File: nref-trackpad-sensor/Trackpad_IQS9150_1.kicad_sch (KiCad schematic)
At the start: 44 parts, among them CN1 FPC_6PIN, IC1 IQS9150-000QFR

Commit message: trackpad: pcb traces adjustment for prod
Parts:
- CN1: footprint Trackpad_IQS9150:FPC6PIN -> Connector_FFC-FPC:Hirose_FH12-6S-0.5SH_1x06-1MP_P0.50mm_Horizontal

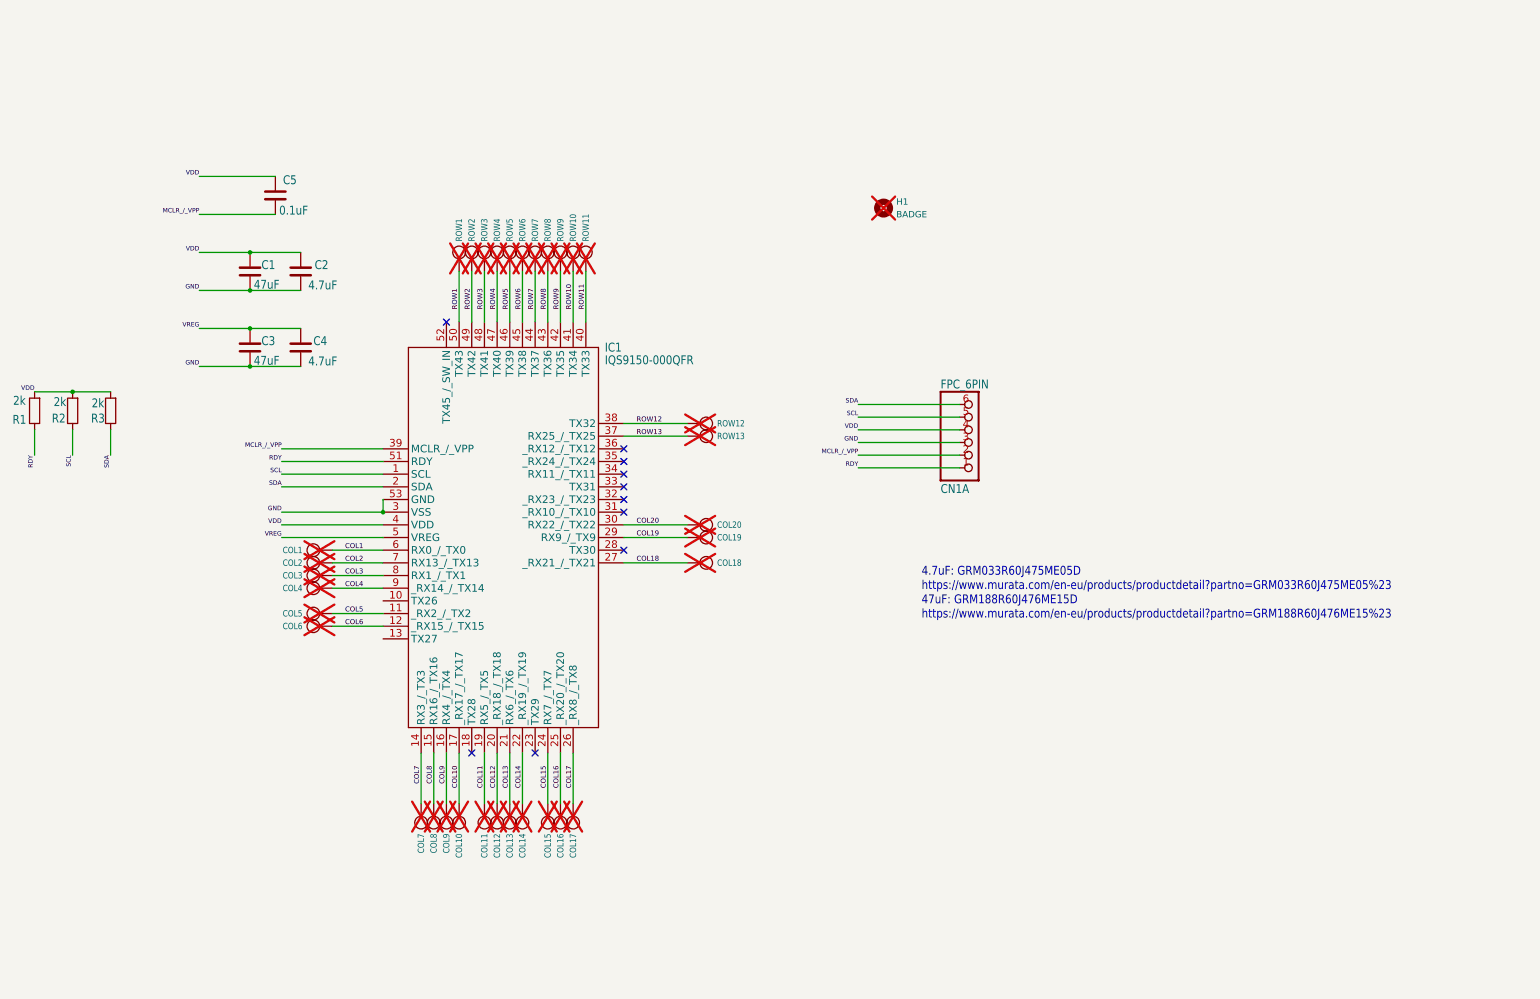
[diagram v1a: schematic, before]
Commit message: clean up major schematics for book
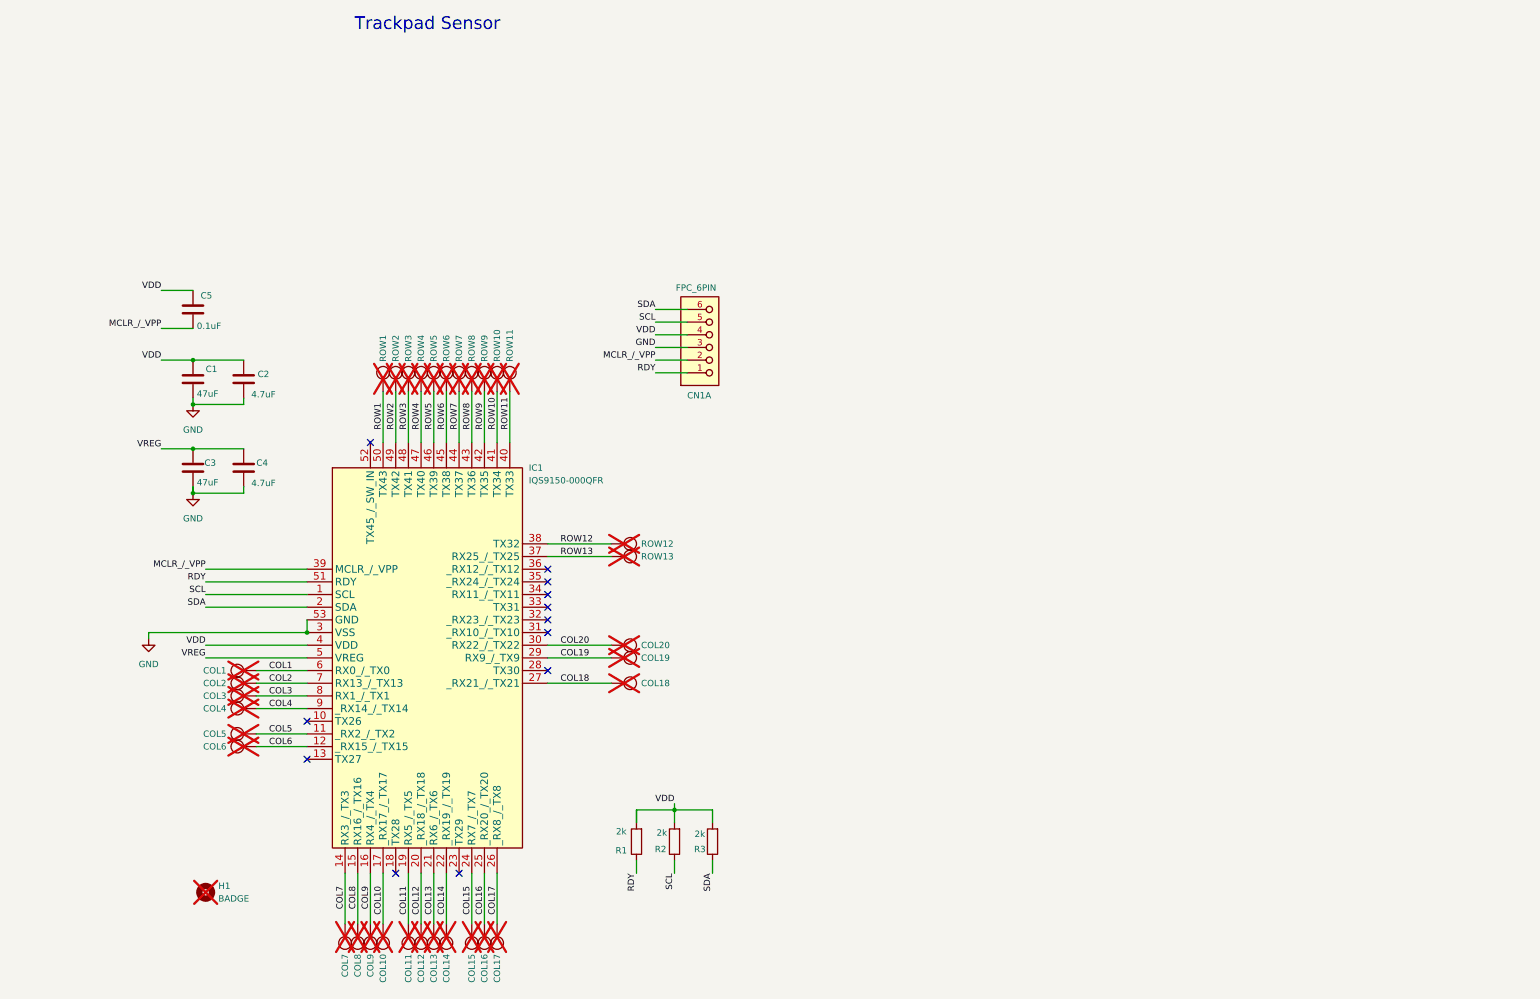
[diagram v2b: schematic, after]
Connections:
- no-connect marks 10 -> 12
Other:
- note added: "Trackpad Sensor"
- note removed: "4.7uF: GRM033R60J475ME05D https://www.murata.com/en-eu/products/productdetail?partno=GRM033R60J475ME05%23 47uF: GRM188R60J476ME15D https://www.murata.com/en-eu/products/productdetail?partno=GRM188R60J476ME15%23"
- company: (none) -> MNT Research GmbH, Copyright 2026
- title: (none) -> MNT Reform Next Trackpad
- moved on the sheet: C1, C2, C3, C4, C5, COL1, COL10, COL11, COL12, COL13, COL14, COL15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
